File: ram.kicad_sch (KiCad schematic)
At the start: 8 parts, among them U10 HyperRAM

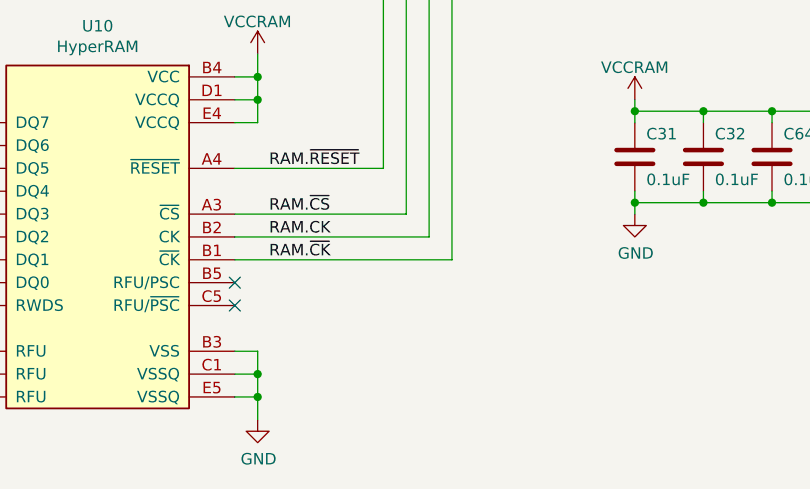
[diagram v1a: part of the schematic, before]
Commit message: Hold U10 HyperRAM in reset by default
Previously it was in an unpredictable default state because the RESET
signal had both a weak pull-up in the HyperRAM and a weak pull-down in
the default FPGA configuration. It should now be held in RESET until the
FPGA is ready to turn it on.
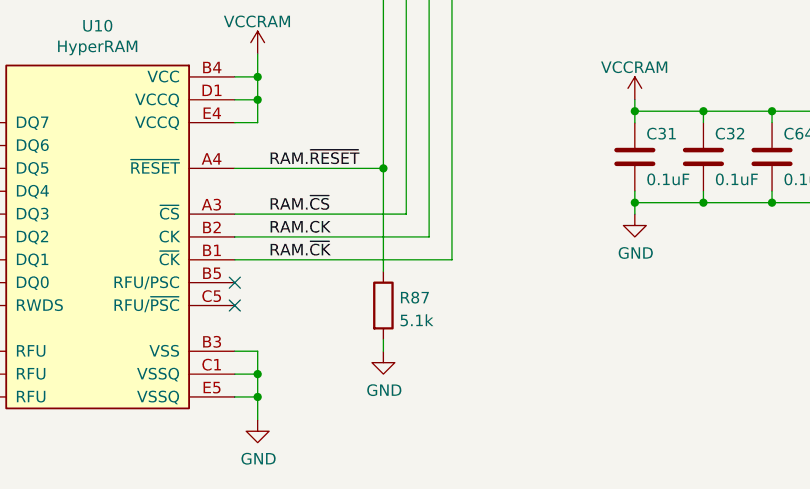
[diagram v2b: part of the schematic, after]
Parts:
- added R87: 5.1k, Resistor_SMD:R_0402_1005Metric, symbol Device:R
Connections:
- net GND: now also R87.2
- net RAM.~{RESET}: now also R87.1
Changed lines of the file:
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@@
   (junction (at 212.09 99.06) (diameter 0) (color 0 0 0 0)
+  )
+  (junction (at 168.91 95.25) (diameter 0) (color 0 0 0 0)
   )
   (junction (at 234.95 88.9) (diameter 0) (color 0 0 0 0)
@@
     (stroke (width 0) (type default))
   )
+  (wire (pts (xy 168.91 95.25) (xy 168.91 106.68))
+    (stroke (width 0) (type default))
+  )
   (wire (pts (xy 168.91 73.66) (xy 168.91 95.25))
     (stroke (width 0) (type default))
@@
   )
   (wire (pts (xy 90.17 107.95) (xy 90.17 73.66))
+    (stroke (width 0) (type default))
+  )
+  (wire (pts (xy 168.91 114.3) (xy 168.91 115.57))
     (stroke (width 0) (type default))
   )
@@
     )
   )
+  (symbol (lib_id "power:GND") (at 168.91 115.57 0) (unit 1)
+    (in_bom yes) (on_board yes) (dnp no)
+    (property "Reference" "#PWR0256" (at 168.91 121.92 0)
+      (effects (font (size 1.27 1.27)) hide)
+    )
+    (property "Value" "GND" (at 169.0116 119.9388 0)
+      (effects (font (size 1.27 1.27)))
+    )
+    (property "Footprint" "" (at 168.91 115.57 0)
+      (effects (font (size 1.27 1.27)) hide)
+    )
+    (property "Datasheet" "" (at 168.91 115.57 0)
+      (effects (font (size 1.27 1.27)) hide)
+    )
+    (pin "1")
+    (instances
+      (project "cynthion"
+        (path "/fb621148-8145-4217-9712-738e1b5a4823/00000000-0000-0000-0000-00005de77fe3"
+          (reference "#PWR0256") (unit 1)
+        )
+      )
+    )
+  )
   (symbol (lib_id "Device:C") (at 227.33 93.98 0) (unit 1)
     (in_bom yes) (on_board yes) (dnp no)
@@
         )
       )
+    )
+  )
+  (symbol (lib_id "Device:R") (at 168.91 110.49 0) (unit 1)
+    (in_bom yes) (on_board yes) (dnp no)
+    (property "Reference" "R87" (at 170.688 109.6553 0)
+      (effects (font (size 1.27 1.27)) (justify left))
+    )
+    (property "Value" "5.1k" (at 170.688 112.1922 0)
+      (effects (font (size 1.27 1.27)) (justify left))
+    )
+    (property "Footprint" "Resistor_SMD:R_0402_1005Metric" (at 167.132 110.49 90)
+      (effects (font (size 1.27 1.27)) hide)
+    )
+    (property "Datasheet" "~" (at 168.91 110.49 0)
+      (effects (font (size 1.27 1.27)) hide)
+    )
+    (property "Part Number" "RC0402JR-075K1L" (at 168.91 110.49 0)
+      (effects (font (size 1.27 1.27)) hide)
+    )
+    (property "Substitution" "any equivalent" (at 168.91 110.49 0)
+      (effects (font (size 1.27 1.27)) hide)
+    )
+    (property "Description" "RES 5.1K OHM 5% 1/16W 0402" (at 168.91 110.49 0)
+      (effects (font (size 1.27 1.27)) hide)
+    )
+    (property "Manufacturer" "Yageo" (at 168.91 110.49 0)
+      (effects (font (size 1.27 1.27)) hide)
+    )
+    (pin "1")
+    (pin "2")
+    (instances
+      (project "cynthion"
+        (path "/fb621148-8145-4217-9712-738e1b5a4823/490fda6e-4eae-4b35-a875-405b51914829"
+          (reference "R87") (unit 1)
+        )
+        (path "/fb621148-8145-4217-9712-738e1b5a4823/00000000-0000-0000-0000-00005de77fe3"
+          (reference "R119") (unit 1)
+        )
+      )

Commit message: opened and saved in KiCad 7.0.10
after upgrading from 7.0.9
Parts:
- renumbered R87 to R119
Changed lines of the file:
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@@
   (symbol (lib_id "Device:R") (at 168.91 110.49 0) (unit 1)
     (in_bom yes) (on_board yes) (dnp no)
-    (property "Reference" "R87" (at 170.688 109.6553 0)
+    (property "Reference" "R119" (at 170.688 109.6553 0)
       (effects (font (size 1.27 1.27)) (justify left))
     )
@@
     (instances
       (project "cynthion"
-        (path "/fb621148-8145-4217-9712-738e1b5a4823/490fda6e-4eae-4b35-a875-405b51914829"
-          (reference "R87") (unit 1)
-        )
         (path "/fb621148-8145-4217-9712-738e1b5a4823/00000000-0000-0000-0000-00005de77fe3"
           (reference "R119") (unit 1)

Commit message: Add S27KL0642DPBHI020 substitution for U10
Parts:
- U10: Substitution W956A8MBYA5I -> W956A8MBYA5I, Infineon S27KL0642DPBHI020
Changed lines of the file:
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@@
       (effects (font (size 1.27 1.27)) hide)
     )
-    (property "Substitution" "W956A8MBYA5I" (at 137.16 102.87 0)
+    (property "Substitution" "W956A8MBYA5I, Infineon S27KL0642DPBHI020" (at 137.16 102.87 0)
       (effects (font (size 1.27 1.27)) hide)
     )

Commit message: Update copyright notices
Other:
- company: Copyright 2019-2023 Great Scott Gadgets -> ${COPYRIGHT}
- title: Cynthion -> ${TITLE}
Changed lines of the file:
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@@
   (paper "A4")
   (title_block
-    (title "Cynthion")
+    (title "${TITLE}")
     (date "${DATE}")
     (rev "${VERSION}")
-    (company "Copyright 2019-2023 Great Scott Gadgets")
-    (comment 1 "Licensed under the CERN-OHL-P v2")
+    (company "${COPYRIGHT}")
+    (comment 1 "${LICENSE}")
   )
   (bus_alias "HyperRAM" (members "DQ[0..7]" "CK" "~{CK}" "~{CS}" "RWDS" "~{RESET}"))
